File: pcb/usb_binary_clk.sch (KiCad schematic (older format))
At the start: 35 parts

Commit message: added part values, shold be done
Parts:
- removed R? (x3): R, symbol Device:R
- added J?: USB_B_Micro, symbol Connector:USB_B_Micro
- added R? (x2): 4.7k, symbol Device:R
- added R? (x4): R, symbol Device:R
- R? (x2): value R -> 47k
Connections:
- net +5V: now also J?.1 (VBUS), R?.2, R?.2
- net GND: now also SW?.2, SW?.2, SW?.2, J?.5 (GND), J?.6 (Shield); no longer R?.2
- net row0: now also R?.2
- net row1: now also R?.2
- net row2: now also R?.2
- net row3: now also R?.2
- net scl: now also R?.1
- net sda: now also R?.1
- net sw: now also R?.1, R?.2; no longer SW?.2, SW?.2, SW?.2
- net at R?.1: now also R?.2, SW?.1; no longer R?.2
- net at R?.1, R?.2: now also SW?.1
- net at R?.2: now also SW?.1; no longer R?.1
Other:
- moved on the sheet: BT?, C?, D?, J?, R?, SW?, U?, Y?

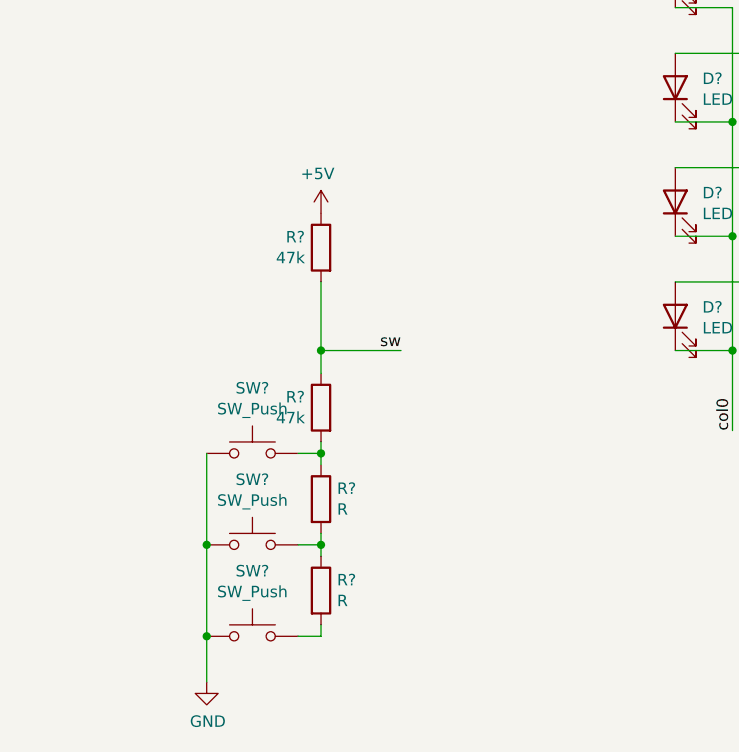
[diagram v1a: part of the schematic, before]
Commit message: resistor ladder fixed
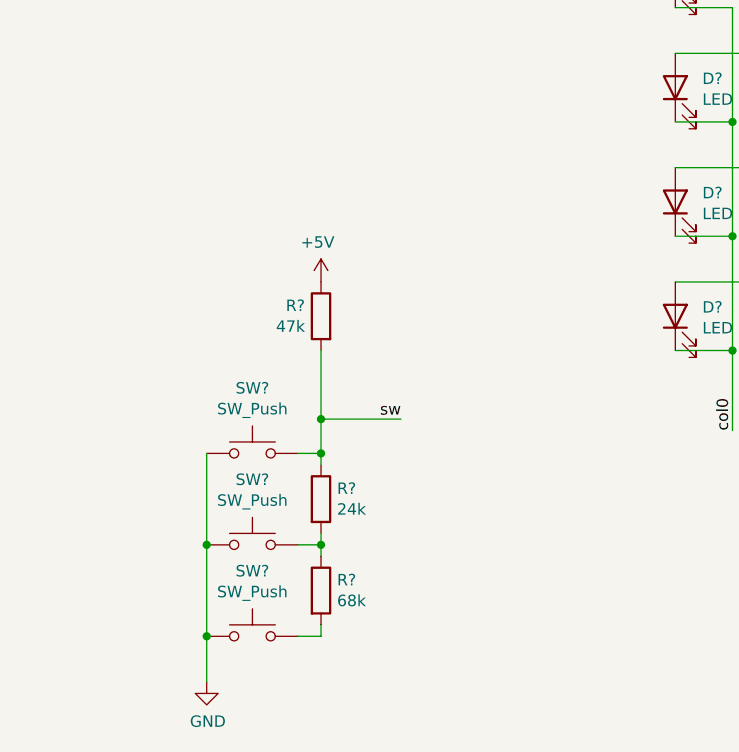
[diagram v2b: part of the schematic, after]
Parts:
- removed R?: 47k, symbol Device:R
- R?: value R -> 24k
- R?: value R -> 68k
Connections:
- net sw: now also R?.1, SW?.1
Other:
- moved on the sheet: R?
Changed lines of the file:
@@
 Text Label 9950 4550 2    50   ~ 0
 scl
-Text Label 2650 5450 2    50   ~ 0
+Text Label 2650 5750 2    50   ~ 0
 sw
 Text Label 9900 4650 2    50   ~ 0
@@
 P 2300 6100
 F 0 "R?" H 2370 6146 50  0000 L CNN
-F 1 "R" H 2370 6055 50  0000 L CNN
+F 1 "24k" H 2370 6055 50  0000 L CNN
 F 2 "" V 2230 6100 50  0001 C CNN
 F 3 "~" H 2300 6100 50  0001 C CNN
@@
 P 2300 6500
 F 0 "R?" H 2370 6546 50  0000 L CNN
-F 1 "R" H 2370 6455 50  0000 L CNN
+F 1 "68k" H 2370 6455 50  0000 L CNN
 F 2 "" V 2230 6500 50  0001 C CNN
 F 3 "~" H 2300 6500 50  0001 C CNN
 	1    2300 6500
 	1    0    0    -1
-$EndComp
-$Comp
-L Device:R R?
-U 1 1 60FE63F1
-P 2300 5700
-F 0 "R?" H 2370 5746 50  0000 L CNN
-F 1 "47k" H 2370 5655 50  0000 L CNN
-F 2 "" V 2230 5700 50  0001 C CNN
-F 3 "~" H 2300 5700 50  0001 C CNN
-	1    2300 5700
-	-1   0    0    -1
 $EndComp
 $Comp
@@
 $EndComp
 Wire Wire Line
-	2300 5450 2650 5450
-Wire Wire Line
-	2300 5450 2300 5550
+	2300 5750 2650 5750
 Wire Wire Line
 	2300 6350 2300 6300
@@
 Connection ~ 2300 5900
 Wire Wire Line
-	2300 5900 2300 5850
-Wire Wire Line
 	1800 6900 1800 6700
 Connection ~ 1800 6300
@@
 Wire Wire Line
 	1800 6700 1800 6300
-Connection ~ 2300 5450
-Wire Wire Line
-	2300 5150 2300 5450
+Connection ~ 2300 5750
+Wire Wire Line
+	2300 5450 2300 5750
 $Comp
 L Device:R R?
 U 1 1 61255740
-P 2300 5000
-F 0 "R?" H 2370 5046 50  0000 L CNN
-F 1 "47k" H 2370 4955 50  0000 L CNN
-F 2 "" V 2230 5000 50  0001 C CNN
-F 3 "~" H 2300 5000 50  0001 C CNN
-	1    2300 5000
+P 2300 5300
+F 0 "R?" H 2370 5346 50  0000 L CNN
+F 1 "47k" H 2370 5255 50  0000 L CNN
+F 2 "" V 2230 5300 50  0001 C CNN
+F 3 "~" H 2300 5300 50  0001 C CNN
+	1    2300 5300
 	-1   0    0    -1
 $EndComp
@@
 L power:+5V #PWR?
 U 1 1 60FF7A20
-P 2300 4850
-F 0 "#PWR?" H 2300 4700 50  0001 C CNN
-F 1 "+5V" H 2315 5023 50  0000 C CNN
-F 2 "" H 2300 4850 50  0001 C CNN
-F 3 "" H 2300 4850 50  0001 C CNN
-	1    2300 4850
+P 2300 5150
+F 0 "#PWR?" H 2300 5000 50  0001 C CNN
+F 1 "+5V" H 2315 5323 50  0000 C CNN
+F 2 "" H 2300 5150 50  0001 C CNN
+F 3 "" H 2300 5150 50  0001 C CNN
+	1    2300 5150
 	-1   0    0    -1
 $EndComp
+Wire Wire Line
+	2300 5750 2300 5900
 $EndSCHEMATC

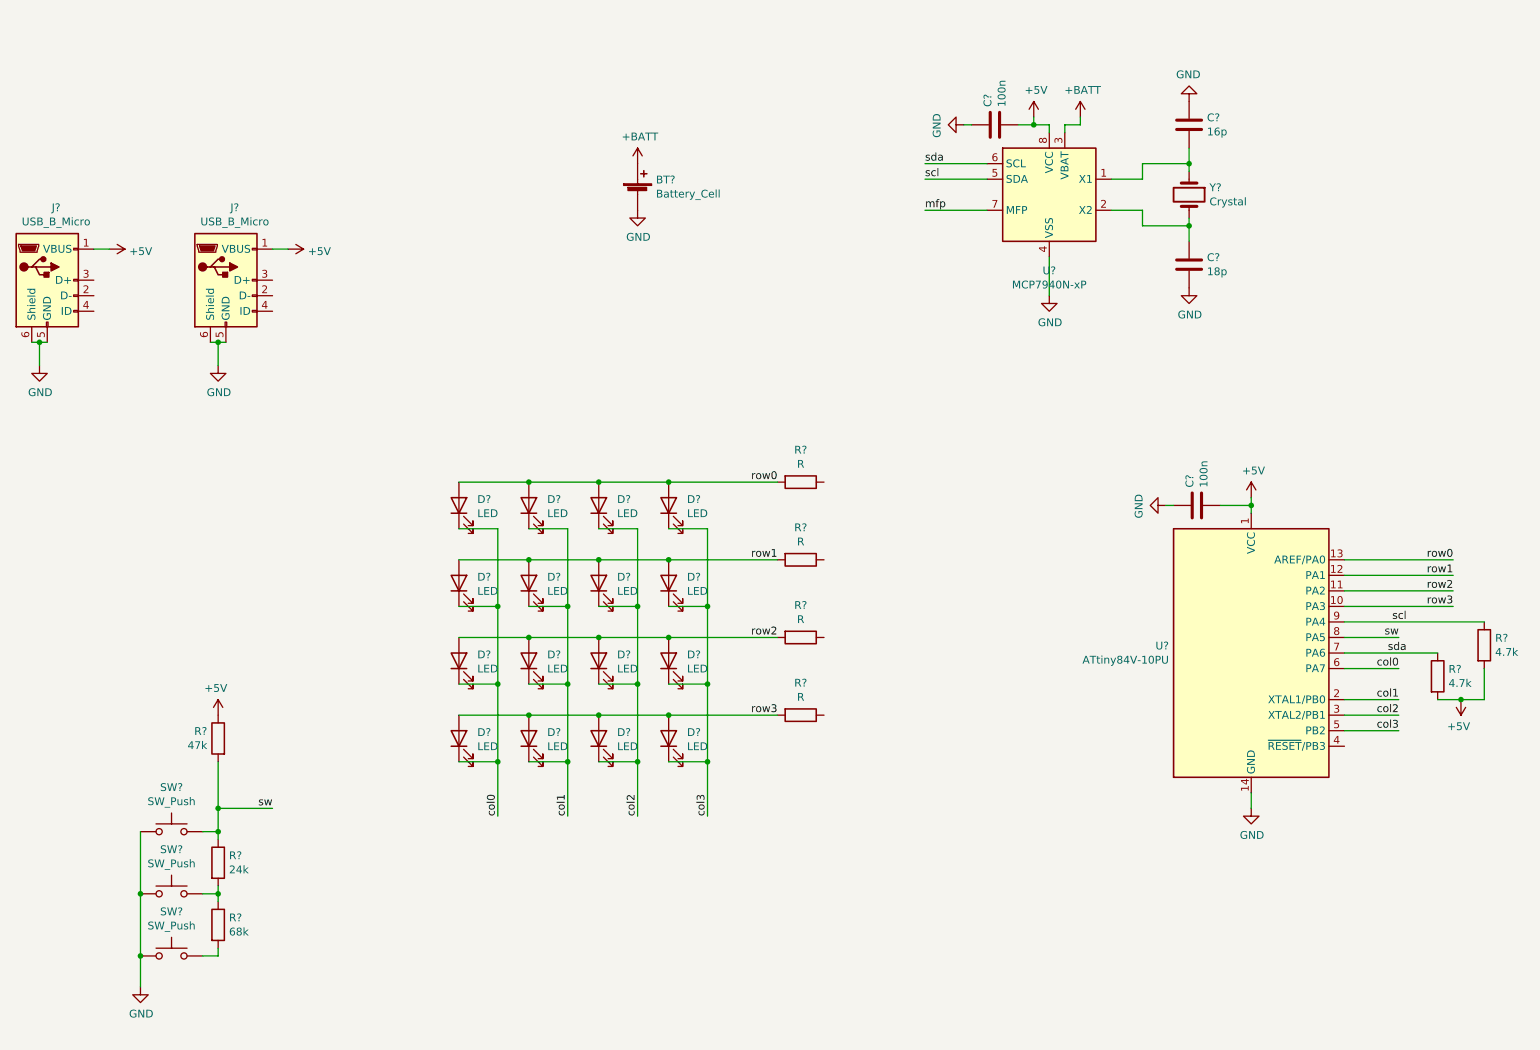
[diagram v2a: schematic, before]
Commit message: Improved led matrix to use up less pins
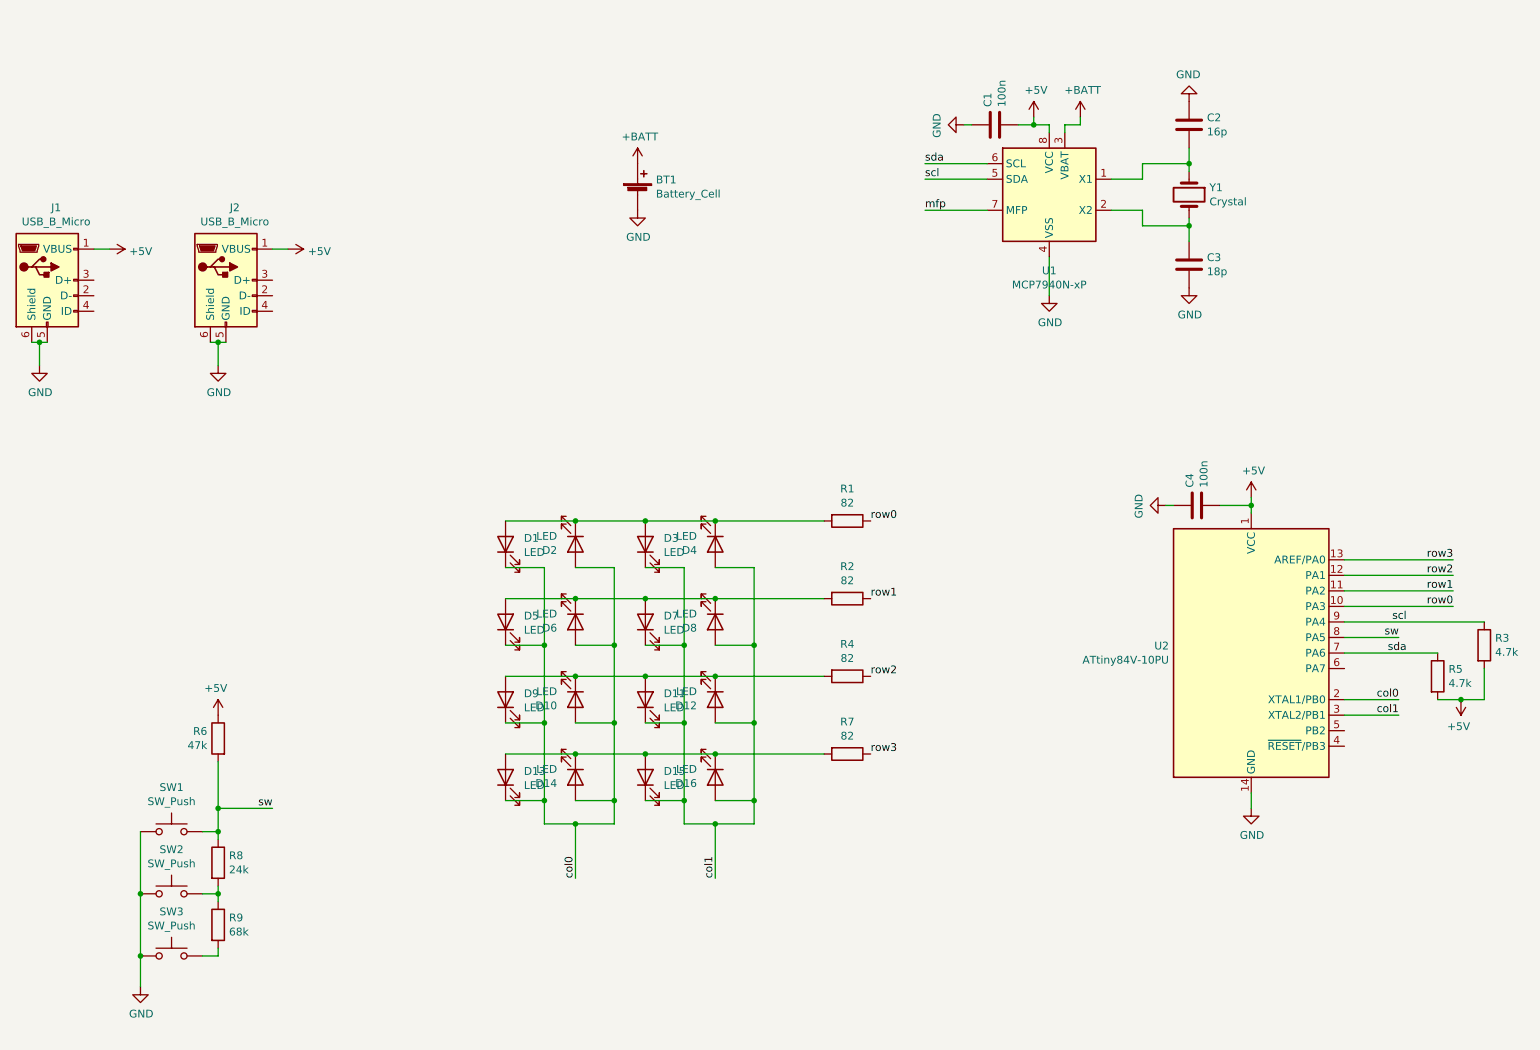
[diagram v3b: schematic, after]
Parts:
- removed D? (x16): LED, symbol Device:LED
- removed R? (x4): R, symbol Device:R
- added D1, D10, D11, D12, D13, D14, D15, D16, D2, D3, D4, D5, D6, D7, D8, D9: LED, symbol Device:LED
- added R1, R2, R4, R7: 82, symbol Device:R
- gave numbers to parts that had none: 18
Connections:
- net col2 is gone; now on net col1: U2.3 (XTAL2/PB1)
- net col0: now also U2.2 (XTAL1/PB0), D1.1 (K), D10.2 (A), D13.1 (K), D14.2 (A), D2.2 (A), D5.1 (K), D6.2 (A), D9.1 (K); no longer U2.6 (PA7)
- net col1: now also D11.1 (K), D12.2 (A), D15.1 (K), D16.2 (A), D3.1 (K), D4.2 (A), D7.1 (K), D8.2 (A); no longer U2.2 (XTAL1/PB0)
- net row0: now also U2.10 (PA3), R1.1; no longer U2.13 (AREF/PA0)
- net row1: now also U2.11 (PA2), R2.1; no longer U2.12 (PA1)
- net row2: now also U2.12 (PA1), R4.1; no longer U2.11 (PA2)
- net row3: now also U2.13 (AREF/PA0), R7.1; no longer U2.10 (PA3)
- net col3: no longer names the net of U2.5 (PB2)
- new net: D13.2 (A), D14.1 (K), D15.2 (A), D16.1 (K), R7.2
- new net: D10.1 (K), D11.2 (A), D12.1 (K), D9.2 (A), R4.2
- new net: D5.2 (A), D6.1 (K), D7.2 (A), D8.1 (K), R2.2
- new net: D1.2 (A), D2.1 (K), D3.2 (A), D4.1 (K), R1.2

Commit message: added phototransistor
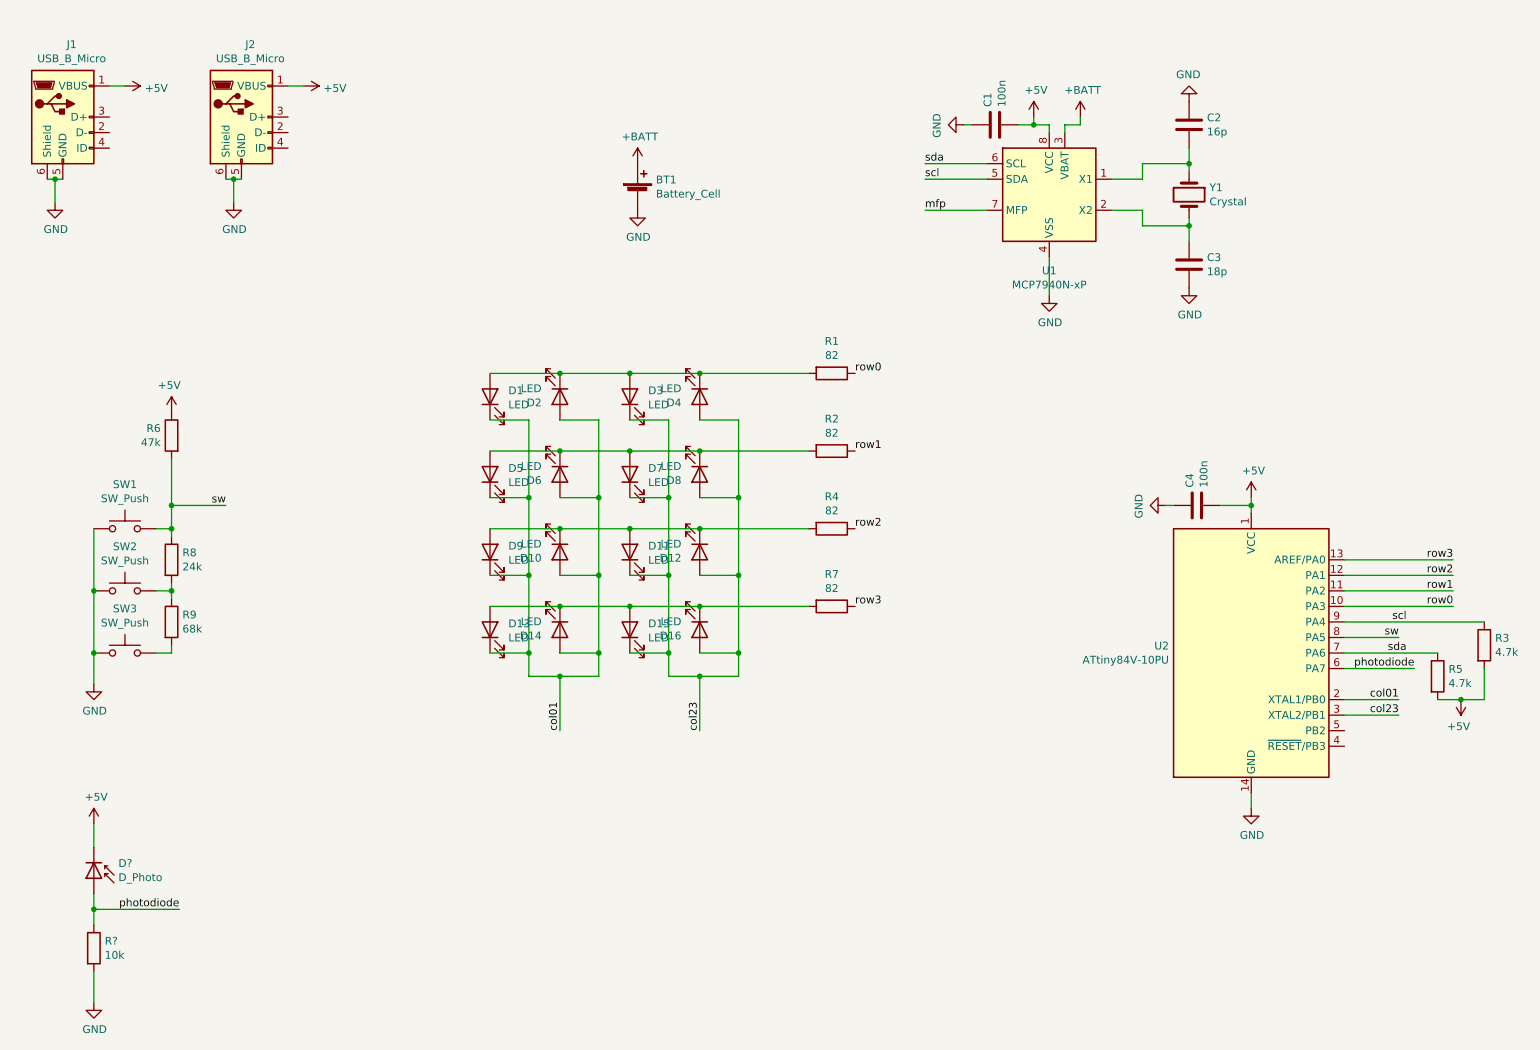
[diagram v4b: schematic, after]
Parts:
- added D?: D_Photo, symbol Device:D_Photo
- added R?: 10k, symbol Device:R
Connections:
- net +5V: now also D?.1 (K)
- net GND: now also R?.2
- net photodiode: now reaches U2.6 (PA7)
- net photodiode: now also D?.2 (A), R?.1
- net col0 renamed col01
- net col1 renamed col23
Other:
- moved on the sheet: D1, D10, D11, D12, D13, D14, D15, D16, D2, D3, D4, D5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

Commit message: linked symbols to footprints, started arranging/modding them
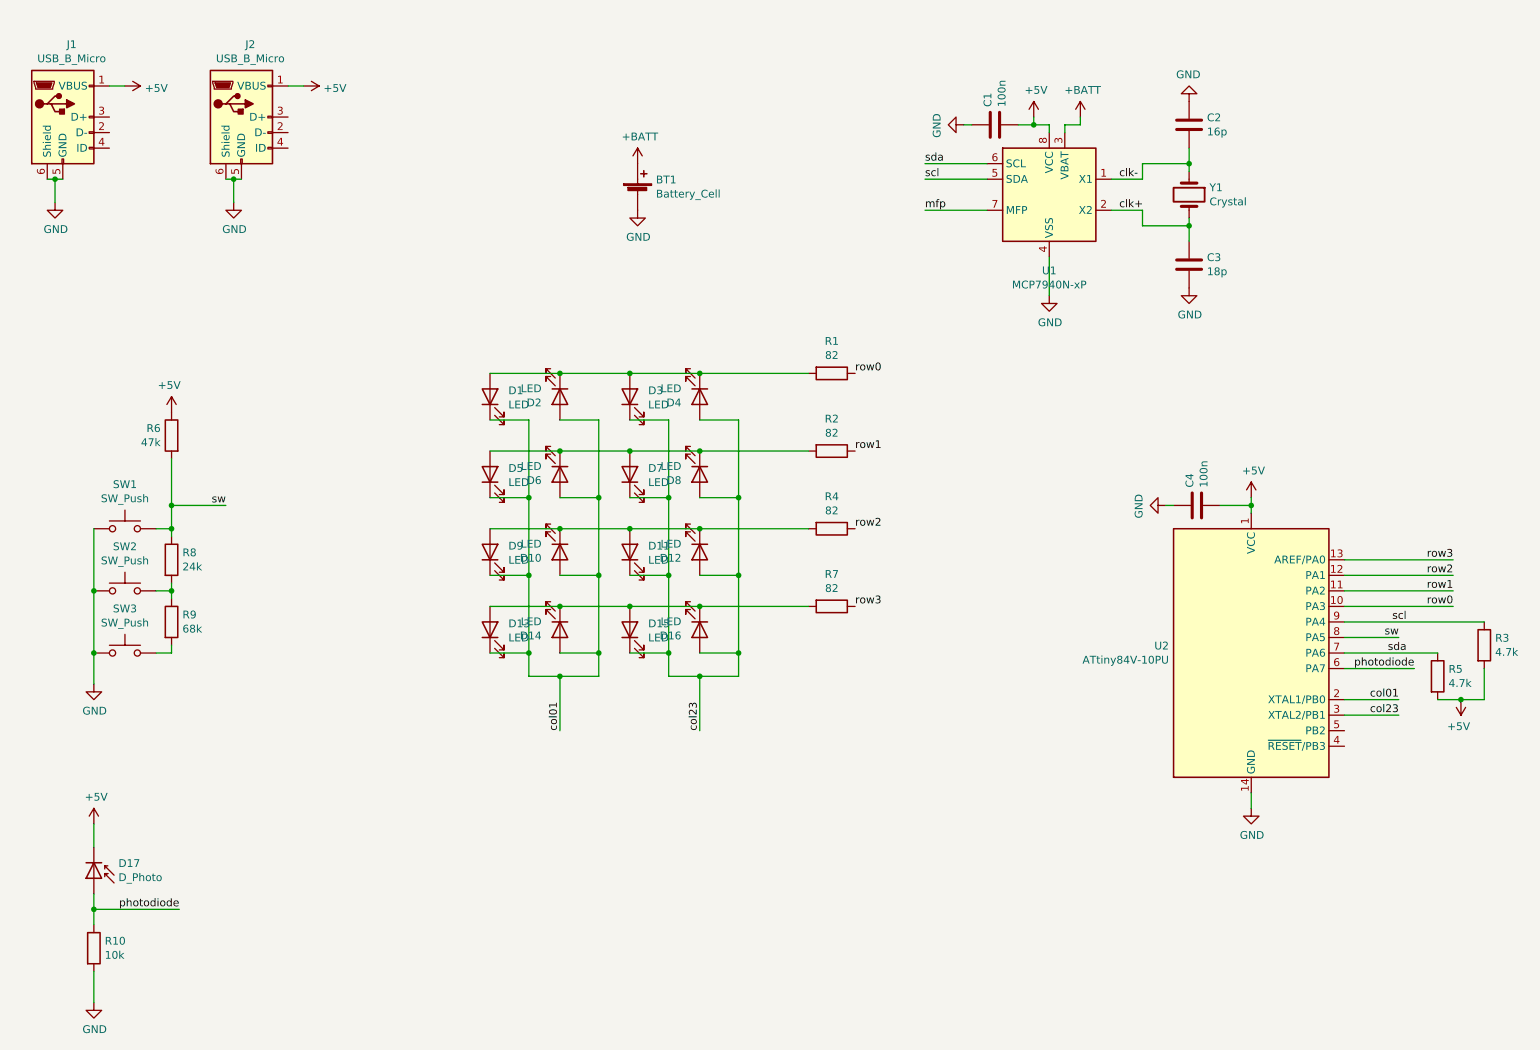
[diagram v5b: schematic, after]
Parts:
- BT1: footprint (none) -> Battery:BatteryHolder_Keystone_3001_1x12mm
- C1, C2, C3, C4: footprint (none) -> Capacitor_THT:C_Disc_D4.3mm_W1.9mm_P5.00mm
- D1, D10, D11, D12, D13, D14, D15, D16, D2, D3, D4, D5, D6, D7, D8, D9: footprint (none) -> custom:LED_D5.0mm
- D17: renamed from D?; footprint (none) -> custom:LED_D5.0mm
- J1, J2: footprint (none) -> Connector_USB:USB_Micro-B_GCT_USB3076-30-A
- R1, R2, R3, R4, R5, R6, R7, R8, R9: footprint (none) -> Resistor_THT:R_Axial_DIN0204_L3.6mm_D1.6mm_P7.62mm_Horizontal
- R10: renamed from R?; footprint (none) -> Resistor_THT:R_Axial_DIN0204_L3.6mm_D1.6mm_P7.62mm_Horizontal
- SW1, SW2, SW3: footprint (none) -> custom:SW_PUSH_6mm_H4.3mm
- U1: footprint (none) -> Package_DIP:DIP-8_W7.62mm
- Y1: footprint (none) -> Crystal:Crystal_AT310_D3.0mm_L10.0mm_Horizontal
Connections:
- net clk-: now reaches C2.2, U1.1 (X1), Y1.1
- net clk+: now reaches C3.1, U1.2 (X2), Y1.2
